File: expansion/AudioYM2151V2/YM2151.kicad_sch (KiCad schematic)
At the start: 21 parts, among them U2 LTC6903, U3 YM2151, U4 YM3012, U5 TL064

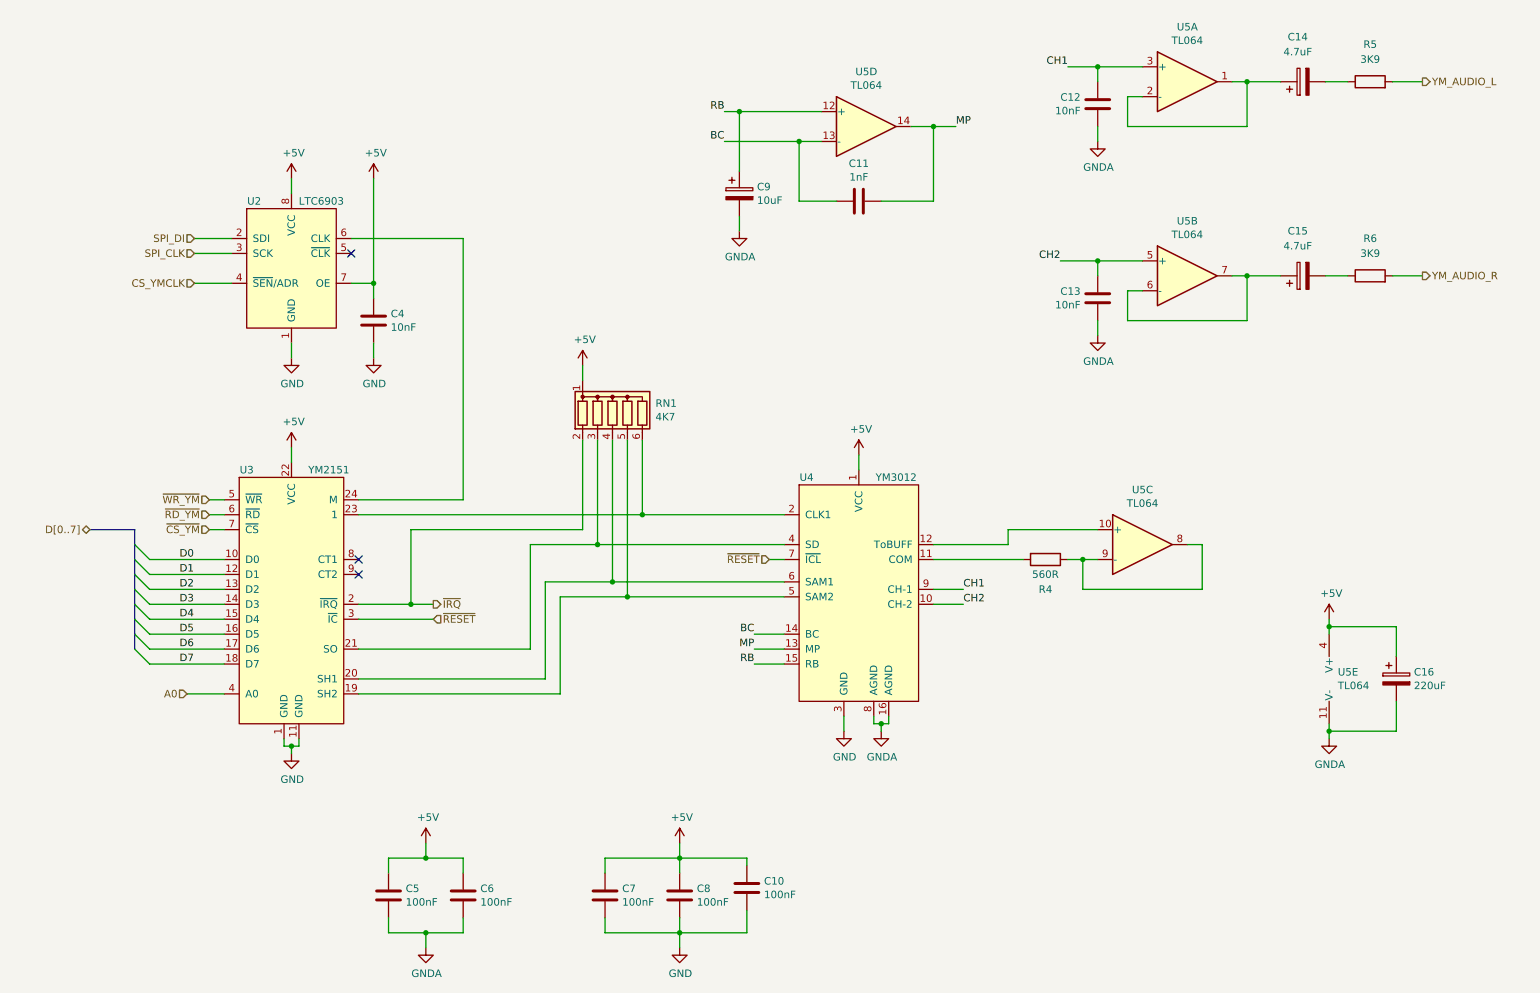
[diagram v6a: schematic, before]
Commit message: Working on footprint positions
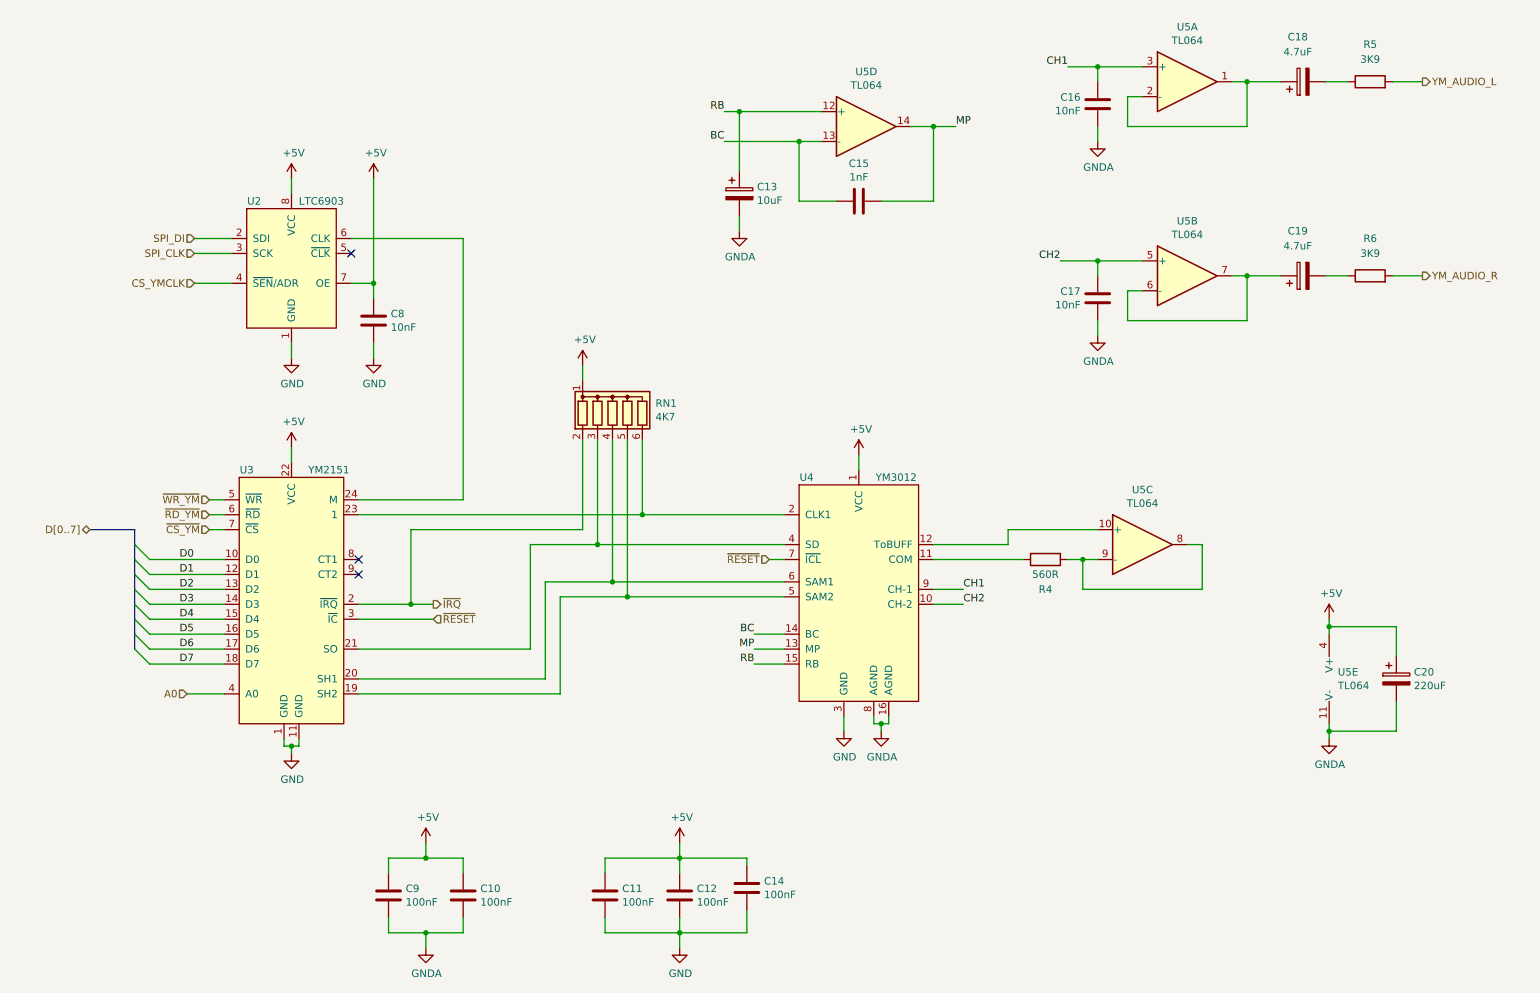
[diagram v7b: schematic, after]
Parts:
- renumbered C6 to C10, C7 to C11, C8 to C12, C9 to C13, C10 to C14, C11 to C15, C12 to C16, C13 to C17, C14 to C18, C15 to C19, C16 to C20, C4 to C8, C5 to C9

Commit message: YM 2151 changes
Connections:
- net A0 renamed CPU_A0
- net D0 renamed CPU_D0
- net D1 renamed CPU_D1
- net D2 renamed CPU_D2
- net D3 renamed CPU_D3
- net D4 renamed CPU_D4
- net D5 renamed CPU_D5
- net D6 renamed CPU_D6
- net D7 renamed CPU_D7
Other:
- moved on the sheet: C10, C11, C12, C13, C14, C15, C16, C17, C18, C19, C20, C8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
